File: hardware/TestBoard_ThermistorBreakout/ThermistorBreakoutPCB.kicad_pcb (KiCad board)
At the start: 2 copper layers, 24.8 x 22.2 mm, 15 parts, among them J1 Conn_01x02, J2 Conn_01x03, J8 Conn_01x06

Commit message: redid thermistor board
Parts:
- removed J2: Conn_01x03, Connector_PinHeader_2.54mm:PinHeader_1x03_P2.54mm_Horizontal
- removed R1, R2, R3, R4: 6.49k, Resistor_SMD:R_0603_1608Metric_Pad0.98x0.95mm_HandSolder
- removed TH1, TH2, TH3, TH4: Thermistor_NTC, UTSVT_Special:THERM_ERT-J1VR104FM
- removed TP1, TP2, TP3, TP4: TestPoint, TestPoint:TestPoint_Keystone_5005-5009_Compact
- added J3: Conn_01x03, Connector_PinHeader_2.54mm:PinHeader_1x03_P2.54mm_Vertical, F.Cu at (131.2, 40.2)
- added J4: Conn_01x03, Connector_PinHeader_2.54mm:PinHeader_1x03_P2.54mm_Vertical, F.Cu at (124.0, 40.2)
- added J5: Conn_01x03, Connector_PinHeader_2.54mm:PinHeader_1x03_P2.54mm_Vertical, F.Cu at (116.8, 40.2)
- added J6: Conn_01x03, Connector_PinHeader_2.54mm:PinHeader_1x03_P2.54mm_Vertical, F.Cu at (109.5, 40.2)
- added R10: 6.49k, Resistor_SMD:R_0603_1608Metric_Pad0.98x0.95mm_HandSolder, F.Cu at (112.2, 43.5)
- added R11: 6.49k, Resistor_SMD:R_0603_1608Metric_Pad0.98x0.95mm_HandSolder, F.Cu at (114.0, 44.2)
- added R12: 6.49k, Resistor_SMD:R_0603_1608Metric_Pad0.98x0.95mm_HandSolder, F.Cu at (106.8, 44.2)
- added R5: 6.49k, Resistor_SMD:R_0603_1608Metric_Pad0.98x0.95mm_HandSolder, F.Cu at (128.5, 44.2)
- added R6: 6.49k, Resistor_SMD:R_0603_1608Metric_Pad0.98x0.95mm_HandSolder, F.Cu at (134.0, 43.5)
- added R7: 6.49k, Resistor_SMD:R_0603_1608Metric_Pad0.98x0.95mm_HandSolder, F.Cu at (126.8, 43.5)
- added R8: 6.49k, Resistor_SMD:R_0603_1608Metric_Pad0.98x0.95mm_HandSolder, F.Cu at (121.2, 44.2)
- added R9: 6.49k, Resistor_SMD:R_0603_1608Metric_Pad0.98x0.95mm_HandSolder, F.Cu at (119.5, 43.5)
- added TH5: Thermistor_NTC, UTSVT_Special:THERM_ERT-J1VR104FM, F.Cu at (128.5, 40.7)
- added TH6: Thermistor_NTC, UTSVT_Special:THERM_ERT-J1VR104FM, F.Cu at (121.2, 40.7)
- added TH7: Thermistor_NTC, UTSVT_Special:THERM_ERT-J1VR104FM, F.Cu at (114.0, 40.7)
- added TH8: Thermistor_NTC, UTSVT_Special:THERM_ERT-J1VR104FM, F.Cu at (106.8, 40.7)
- added TP10: TestPoint, TestPoint:TestPoint_Keystone_5005-5009_Compact, F.Cu at (122.8, 49.6)
- added TP11: TestPoint, TestPoint:TestPoint_Keystone_5005-5009_Compact, F.Cu at (127.2, 49.6)
- added TP8: TestPoint, TestPoint:TestPoint_Keystone_5005-5009_Compact, F.Cu at (118.8, 49.6)
- added TP9: TestPoint, TestPoint:TestPoint_Keystone_5005-5009_Compact, F.Cu at (114.5, 49.6)
- moved J8 8.43 mm to (127.2, 53.4)
- moved J1 4.28 mm to (109.5, 54.2)
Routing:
- net /Temperature1: track 27.7 -> 19.3 mm
- net VDDA: track 54.0 -> 61.1 mm, vias 0 -> 1
- net /Temperature2: track 11.1 -> 16.2 mm
- net /Temperature4: track 11.9 -> 16.1 mm
- net /Temperature3: track 11.2 -> 14.3 mm
- net Net-(J3-Pin_1): track 0.00 -> 2.86 mm
- net Net-(J6-Pin_1): track 0.00 -> 2.86 mm
- net Net-(J5-Pin_1): track 0.00 -> 2.86 mm
- net Net-(J4-Pin_1): track 0.00 -> 2.86 mm
- net Net-(J6-Pin_3): track 0.00 -> 2.80 mm
- net Net-(J5-Pin_3): track 0.00 -> 2.80 mm
- net Net-(J4-Pin_3): track 0.00 -> 2.80 mm
- net Net-(J3-Pin_3): track 0.00 -> 2.80 mm
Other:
- board size 24.8 x 22.2 mm -> 30 x 25 mm
- board text added: "VDD"
- board text removed: "+"
- board text removed: "-"
- board text removed: "1"
- board text removed: "2"
- board text removed: "3"
- board text removed: "3v3"
- board text removed: "4"

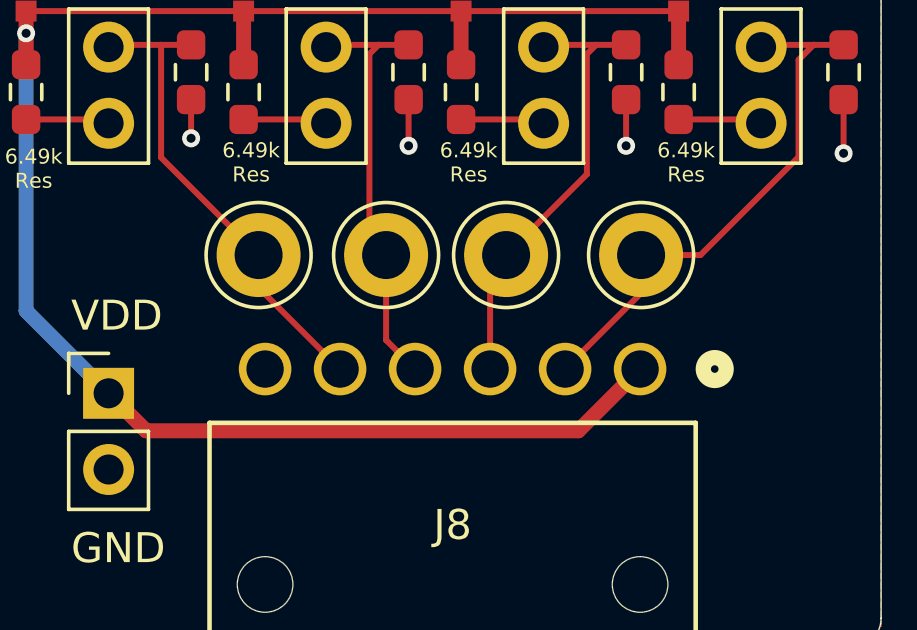
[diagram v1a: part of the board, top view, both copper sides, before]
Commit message: forgot silkscreen
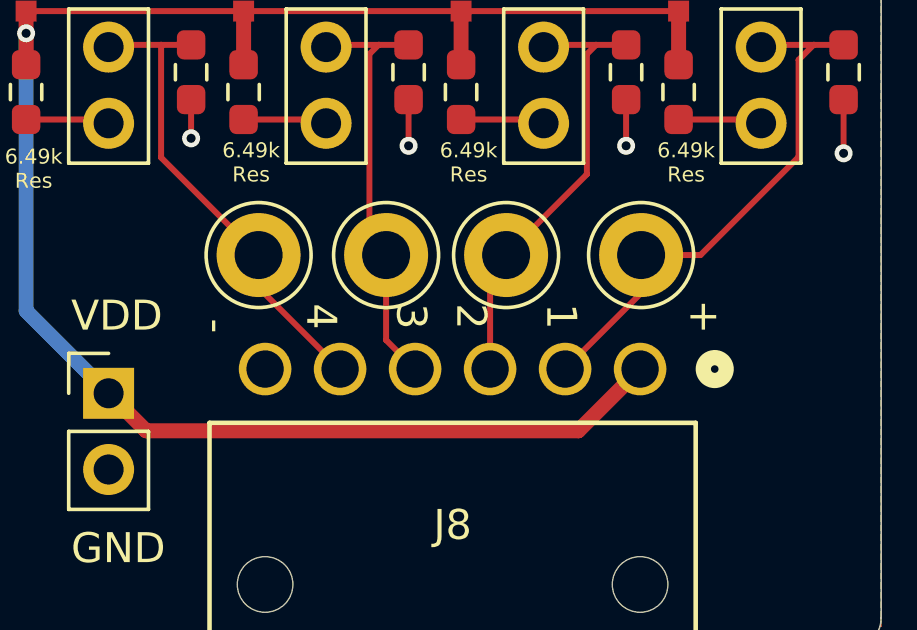
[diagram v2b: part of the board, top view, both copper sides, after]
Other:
- board text added: "+"
- board text added: "-"
- board text added: "1"
- board text added: "2"
- board text added: "3"
- board text added: "4"
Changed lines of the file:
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@@
+		)
+	)
+	(gr_text "+"
+		(at 128.75 52.25 0)
+		(layer "F.SilkS")
+		(effects
+			(font
+				(size 1 1)
+				(thickness 0.15)
+			)
+			(justify left bottom)
+		)
+	)
+	(gr_text "1"
+		(at 124 51.25 270)
+		(layer "F.SilkS")
+		(effects
+			(font
+				(size 1 1)
+				(thickness 0.15)
+			)
+			(justify left bottom)
 		)
 	)
@@
 		)
 	)
+	(gr_text "-"
+		(at 113.5 52.25 90)
+		(layer "F.SilkS")
+		(effects
+			(font
+				(size 1 1)
+				(thickness 0.15)
+			)
+			(justify left bottom)
+		)
+	)
+	(gr_text "2"
+		(at 121 51.25 270)
+		(layer "F.SilkS")
+		(effects
+			(font
+				(size 1 1)
+				(thickness 0.15)
+			)
+			(justify left bottom)
+		)
+	)
 	(gr_text "GND"
 		(at 108.25 60 0)
@@
 				(size 1 1)
 				(thickness 0.1)
+			)
+			(justify left bottom)
+		)
+	)
+	(gr_text "3"
+		(at 119 51.25 270)
+		(layer "F.SilkS")
+		(effects
+			(font
+				(size 1 1)
+				(thickness 0.15)
 			)
 			(justify left bottom)
@@
 		)
 	)
+	(gr_text "4"
+		(at 116 51.25 270)
+		(layer "F.SilkS")
+		(effects
+			(font
+				(size 1 1)
+				(thickness 0.15)
+			)
+			(justify left bottom)
+		)
+	)
